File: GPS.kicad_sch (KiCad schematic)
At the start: 13 parts, among them J3 SMA_180C, Q5 BC817

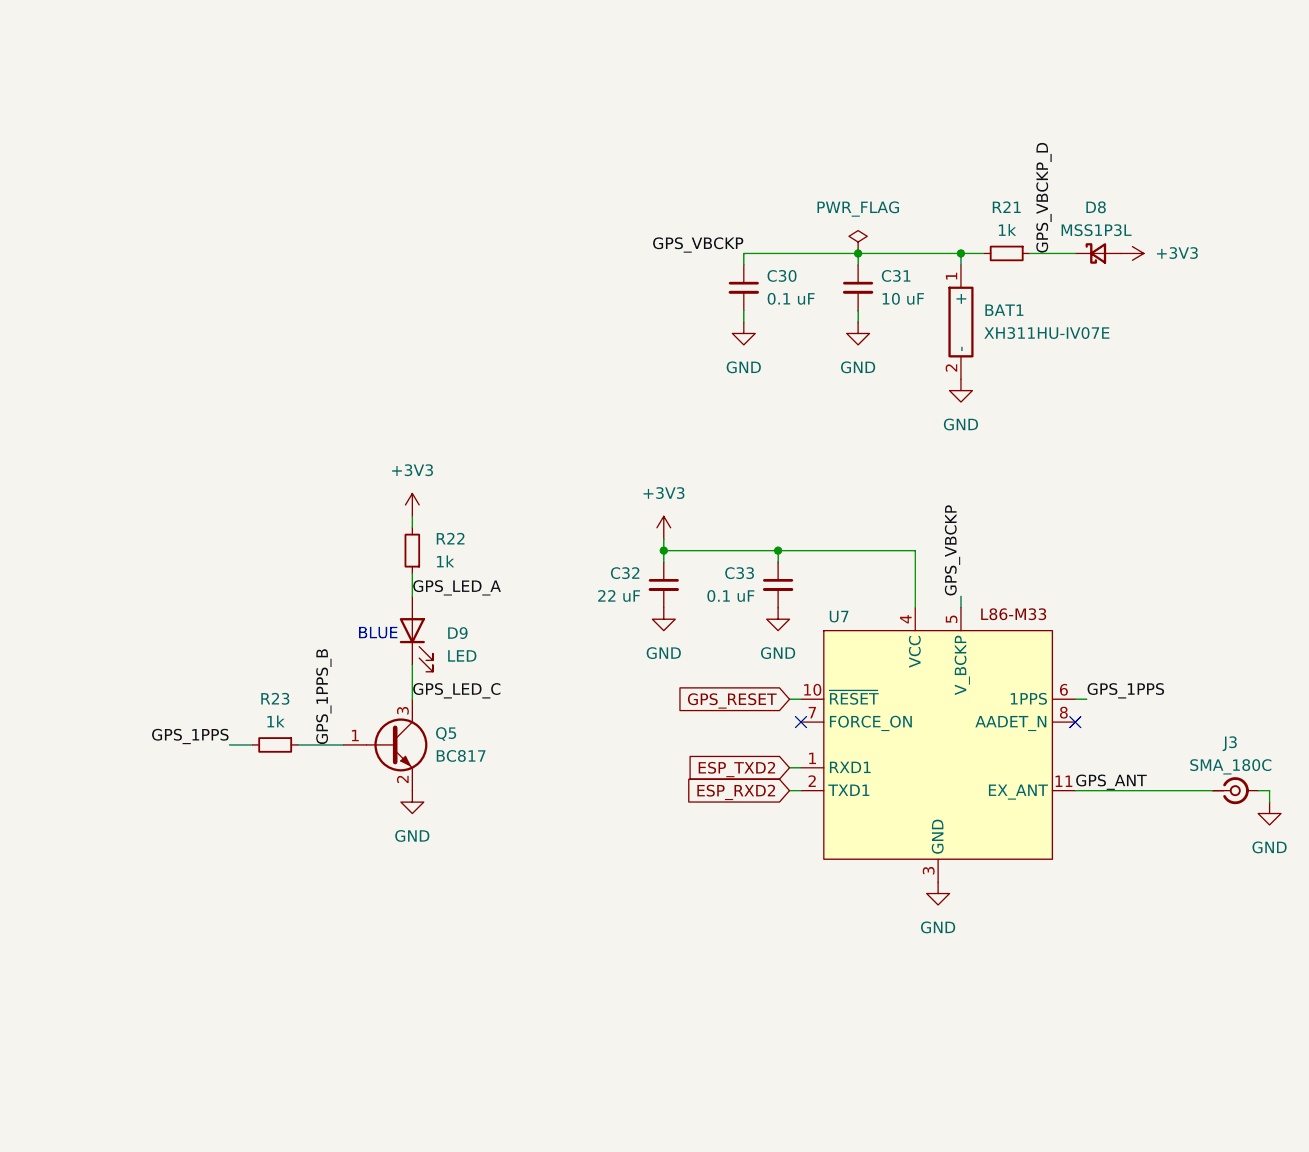
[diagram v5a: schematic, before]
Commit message: Added more graphics, removed some unnecessary features. moved GPU passive components upper. added switching components to LoRa.
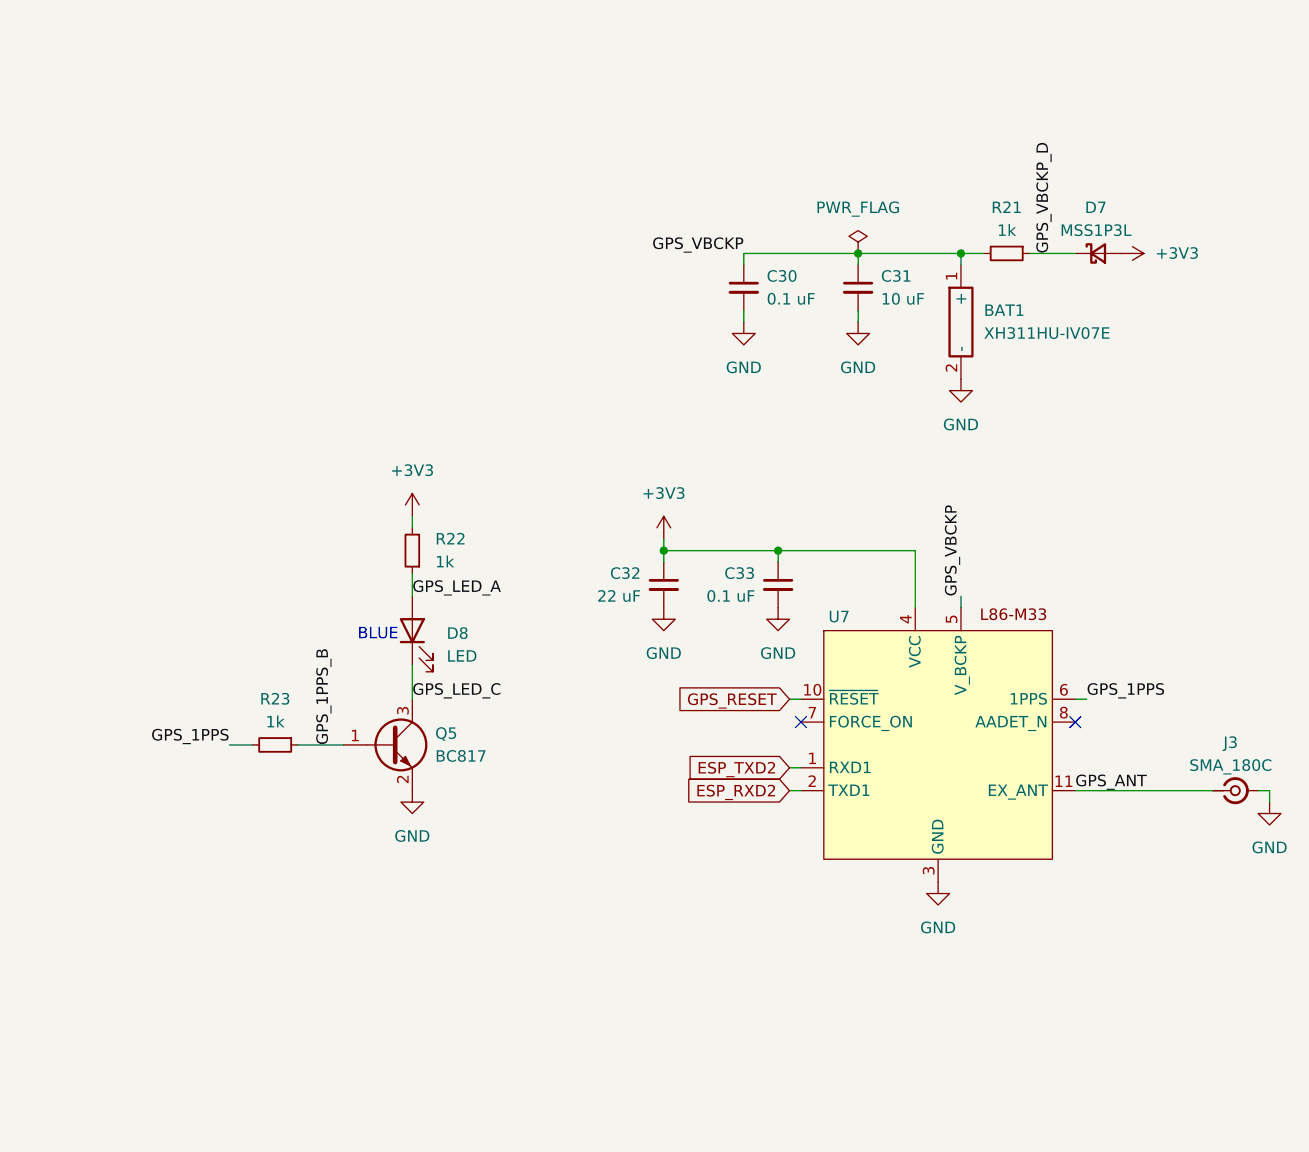
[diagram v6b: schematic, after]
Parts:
- renumbered D8 to D7, D9 to D8
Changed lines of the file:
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@@
 		(dnp no)
 		(fields_autoplaced yes)
-		(property "Reference" "D9"
+		(property "Reference" "D8"
 			(at 95.25 86.6774 90)
 			(effects
@@
 			(project "valkyriev3"
 				(path "/d24fd15c-a242-4d26-9876-7755ca0d378c/00fc6d2a-79f7-4b02-8c94-ea393adce81b"
-					(reference "D9")
+					(reference "D8")
 					(unit 1)
 				)
@@
 		(on_board yes)
 		(dnp no)
-		(property "Reference" "D8"
+		(property "Reference" "D7"
 			(at 167.386 39.37 0)
 			(effects
@@
 			(project ""
 				(path "/d24fd15c-a242-4d26-9876-7755ca0d378c/00fc6d2a-79f7-4b02-8c94-ea393adce81b"
-					(reference "D8")
-					(unit 1)
-				)
+					(reference "D7")
+					(unit 1)
+				)
